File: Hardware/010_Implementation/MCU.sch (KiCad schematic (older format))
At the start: 21 parts, among them J1 2606-3356, J2 Conn_02x05_Odd_Even, SW1 SW_Push, U2 ESP32-DEVKITC-32D

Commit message: Board Version 5
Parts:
- C12, C13, C14, C15: footprint (none) -> Capacitor_SMD:C_0603_1608Metric_Pad1.08x0.95mm_HandSolder
- C8: footprint Capacitor_SMD:C_0603_1608Metric_Pad1.05x0.95mm_HandSolder -> Capacitor_SMD:C_0603_1608Metric_Pad1.08x0.95mm_HandSolder
- D2: Field4 2.65 mm -> (none)
- D3, D4, D5, SW1: Vorhanden (none) -> Yes
- J2: value Conn_02x05_Odd_Even -> JTAG Jumper Pins; Vorhanden (none) -> Yes
- R10, R11, R12, R13, R14, R15, R9: footprint Resistor_SMD:R_0805_2012Metric_Pad1.15x1.40mm_HandSolder -> Resistor_SMD:R_0603_1608Metric_Pad0.98x0.95mm_HandSolder
- R8: value 2.2k -> 1k; footprint Resistor_SMD:R_0805_2012Metric_Pad1.15x1.40mm_HandSolder -> Resistor_SMD:R_0603_1608Metric_Pad0.98x0.95mm_HandSolder
- U2: Field4 4 -> (none); Vorhanden (none) -> Yes
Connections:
- net OBD-CAN_Switch renamed ~OBD~\CAN
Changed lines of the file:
@@
 F 2 "Button_Switch_SMD:SW_Push_1P1T_NO_CK_KSC7xxJ" H 3525 6250 50  0001 C CNN
 F 3 "~" H 3525 6250 50  0001 C CNN
+F 4 "Yes" H 3525 6050 50  0001 C CNN "Vorhanden"
 	1    3525 6050
 	0    -1   -1   0
@@
 F 0 "C8" H 4265 6071 50  0000 L CNN
 F 1 "100n" H 4265 5980 50  0000 L CNN
-F 2 "Capacitor_SMD:C_0603_1608Metric_Pad1.05x0.95mm_HandSolder" H 4188 5875 50  0001 C CNN
+F 2 "Capacitor_SMD:C_0603_1608Metric_Pad1.08x0.95mm_HandSolder" H 4188 5875 50  0001 C CNN
 F 3 "~" H 4150 6025 50  0001 C CNN
 	1    4150 6025
@@
 P 9100 5025
 F 0 "J2" H 9150 4600 50  0000 C CNN
-F 1 "Conn_02x05_Odd_Even" H 9150 4691 50  0000 C CNN
+F 1 "JTAG Jumper Pins" H 9150 4691 50  0000 C CNN
 F 2 "Connector_PinHeader_1.00mm:PinHeader_2x05_P1.00mm_Vertical" H 9100 5025 50  0001 C CNN
 F 3 "~" H 9100 5025 50  0001 C CNN
+F 4 "Yes" H 9100 5025 50  0001 C CNN "Vorhanden"
 	1    9100 5025
 	-1   0    0    1
@@
 F 0 "R9" V 7468 4625 50  0000 C CNN
 F 1 "100" V 7559 4625 50  0000 C CNN
-F 2 "Resistor_SMD:R_0805_2012Metric_Pad1.15x1.40mm_HandSolder" V 7605 4625 50  0001 C CNN
+F 2 "Resistor_SMD:R_0603_1608Metric_Pad0.98x0.95mm_HandSolder" V 7605 4625 50  0001 C CNN
 F 3 "~" H 7675 4625 50  0001 C CNN
 	1    7675 4625
@@
 F 0 "R10" V 7468 4925 50  0000 C CNN
 F 1 "100" V 7559 4925 50  0000 C CNN
-F 2 "Resistor_SMD:R_0805_2012Metric_Pad1.15x1.40mm_HandSolder" V 7605 4925 50  0001 C CNN
+F 2 "Resistor_SMD:R_0603_1608Metric_Pad0.98x0.95mm_HandSolder" V 7605 4925 50  0001 C CNN
 F 3 "~" H 7675 4925 50  0001 C CNN
 	1    7675 4925
@@
 F 0 "R11" V 7882 5250 50  0000 C CNN
 F 1 "100" V 7791 5250 50  0000 C CNN
-F 2 "Resistor_SMD:R_0805_2012Metric_Pad1.15x1.40mm_HandSolder" V 7605 5250 50  0001 C CNN
+F 2 "Resistor_SMD:R_0603_1608Metric_Pad0.98x0.95mm_HandSolder" V 7605 5250 50  0001 C CNN
 F 3 "~" H 7675 5250 50  0001 C CNN
 	1    7675 5250
@@
 F 0 "R12" V 7882 5600 50  0000 C CNN
 F 1 "100" V 7791 5600 50  0000 C CNN
-F 2 "Resistor_SMD:R_0805_2012Metric_Pad1.15x1.40mm_HandSolder" V 7605 5600 50  0001 C CNN
+F 2 "Resistor_SMD:R_0603_1608Metric_Pad0.98x0.95mm_HandSolder" V 7605 5600 50  0001 C CNN
 F 3 "~" H 7675 5600 50  0001 C CNN
 	1    7675 5600
@@
 F 2 "LED_THT:LED_D3.0mm" H 7925 2325 50  0001 C CNN
 F 3 "~" H 7925 2325 50  0001 C CNN
+F 4 "Yes" H 7925 2325 50  0001 C CNN "Vorhanden"
 	1    7925 2325
 	0    -1   -1   0
@@
 F 2 "LED_THT:LED_D3.0mm" H 8350 2325 50  0001 C CNN
 F 3 "~" H 8350 2325 50  0001 C CNN
+F 4 "Yes" H 8350 2325 50  0001 C CNN "Vorhanden"
 	1    8350 2325
 	0    -1   -1   0
@@
 F 2 "LED_THT:LED_D3.0mm" H 8775 2325 50  0001 C CNN
 F 3 "~" H 8775 2325 50  0001 C CNN
+F 4 "Yes" H 8775 2325 50  0001 C CNN "Vorhanden"
 	1    8775 2325
 	0    -1   -1   0
@@
 F 0 "R13" H 7995 2846 50  0000 L CNN
 F 1 "500" H 7995 2755 50  0000 L CNN
-F 2 "Resistor_SMD:R_0805_2012Metric_Pad1.15x1.40mm_HandSolder" V 7855 2800 50  0001 C CNN
+F 2 "Resistor_SMD:R_0603_1608Metric_Pad0.98x0.95mm_HandSolder" V 7855 2800 50  0001 C CNN
 F 3 "~" H 7925 2800 50  0001 C CNN
 	1    7925 2800
@@
 F 0 "R14" H 8420 2846 50  0000 L CNN
 F 1 "500" H 8420 2755 50  0000 L CNN
-F 2 "Resistor_SMD:R_0805_2012Metric_Pad1.15x1.40mm_HandSolder" V 8280 2800 50  0001 C CNN
+F 2 "Resistor_SMD:R_0603_1608Metric_Pad0.98x0.95mm_HandSolder" V 8280 2800 50  0001 C CNN
 F 3 "~" H 8350 2800 50  0001 C CNN
 	1    8350 2800
@@
 F 0 "R15" H 8845 2846 50  0000 L CNN
 F 1 "500" H 8845 2755 50  0000 L CNN
-F 2 "Resistor_SMD:R_0805_2012Metric_Pad1.15x1.40mm_HandSolder" V 8705 2800 50  0001 C CNN
+F 2 "Resistor_SMD:R_0603_1608Metric_Pad0.98x0.95mm_HandSolder" V 8705 2800 50  0001 C CNN
 F 3 "~" H 8775 2800 50  0001 C CNN
 	1    8775 2800
@@
 F 1 "ESP32-DEVKITC-32D" H 3595 2085 50  0000 C CNN
 F 2 "Board:MODULE_ESP32-DEVKITC-32D" H 3600 3180 50  0001 L BNN
-F 3 "Espressif Systems" H 3600 3180 50  0001 L BNN
-F 4 "4" H 3600 3180 50  0001 L BNN "Field4"
+F 3 "https://www.espressif.com/sites/default/files/documentation/esp32_technical_reference_manual_en.pdf#603" H 3600 3180 50  0001 L BNN
+F 4 "" H 3600 3180 50  0001 L BNN "Field4"
+F 5 "Yes" H 3600 3180 50  0001 C CNN "Vorhanden"
 	1    3600 3180
 	1    0    0    1
@@
 OBD_Voltage_Check
 Text HLabel 1875 3180 0    50   Output ~ 0
-OBD-CAN_Switch
+~OBD~\CAN
 $Comp
 L Device:R R8
@@
 P 3525 5550
 F 0 "R8" H 3595 5596 50  0000 L CNN
-F 1 "2.2k" H 3595 5505 50  0000 L CNN
-F 2 "Resistor_SMD:R_0805_2012Metric_Pad1.15x1.40mm_HandSolder" V 3455 5550 50  0001 C CNN
+F 1 "1k" H 3595 5505 50  0000 L CNN
+F 2 "Resistor_SMD:R_0603_1608Metric_Pad0.98x0.95mm_HandSolder" V 3455 5550 50  0001 C CNN
 F 3 "~" H 3525 5550 50  0001 C CNN
 	1    3525 5550
@@
 F 1 "SS24" H 1665 1476 50  0000 C CNN
 F 2 "Board:DIOM5336X265N" H 1665 1350 50  0001 L BNN
-F 3 "IPC 7351B" H 1665 1350 50  0001 L BNN
-F 4 "2.65 mm" H 1665 1350 50  0001 L BNN "Field4"
+F 3 "https://www.onsemi.com/pub/Collateral/SS24-D.PDF" H 1665 1350 50  0001 L BNN
+F 4 "" H 1665 1350 50  0001 L BNN "Field4"
 F 5 "ON Semiconductor" H 1665 1350 50  0001 L BNN "Field5"
 F 6 "1.1.2" H 1665 1350 50  0001 L BNN "Field6"
@@
 F 1 "2606-3356" H 1567 4994 60  0000 C CNN
 F 2 "Board:2606-3356" H 1725 5415 60  0001 C CNN
-F 3 "" H 1325 6275 60  0000 C CNN
+F 3 "https://www.wago.com/global/pcb-terminal-blocks-and-pluggable-connectors/pcb-terminal-block/p/2606-3356" H 1325 6275 60  0001 C CNN
 	1    1325 6275
 	-1   0    0    1
@@
 F 0 "C14" H 4845 1601 50  0000 L CNN
 F 1 "100n" H 4845 1510 50  0000 L CNN
-F 2 "" H 4768 1405 50  0001 C CNN
+F 2 "Capacitor_SMD:C_0603_1608Metric_Pad1.08x0.95mm_HandSolder" H 4768 1405 50  0001 C CNN
 F 3 "~" H 4730 1555 50  0001 C CNN
 	1    4730 1555
@@
 F 0 "C15" H 5200 1601 50  0000 L CNN
 F 1 "1u" H 5200 1510 50  0000 L CNN
-F 2 "" H 5123 1405 50  0001 C CNN
+F 2 "Capacitor_SMD:C_0603_1608Metric_Pad1.08x0.95mm_HandSolder" H 5123 1405 50  0001 C CNN
 F 3 "~" H 5085 1555 50  0001 C CNN
 	1    5085 1555
@@
 F 0 "C13" H 2575 1741 50  0000 L CNN
 F 1 "100n" H 2575 1650 50  0000 L CNN
-F 2 "" H 2498 1545 50  0001 C CNN
+F 2 "Capacitor_SMD:C_0603_1608Metric_Pad1.08x0.95mm_HandSolder" H 2498 1545 50  0001 C CNN
 F 3 "~" H 2460 1695 50  0001 C CNN
 	1    2460 1695
@@
 F 0 "C12" H 1990 1741 50  0000 R CNN
 F 1 "1u" H 1990 1650 50  0000 R CNN
-F 2 "" H 2143 1545 50  0001 C CNN
+F 2 "Capacitor_SMD:C_0603_1608Metric_Pad1.08x0.95mm_HandSolder" H 2143 1545 50  0001 C CNN
 F 3 "~" H 2105 1695 50  0001 C CNN
 	1    2105 1695

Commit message: Board Version 7
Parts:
- removed J1: 2606-3356, Board:2606-3356, symbol Board-rescue:2606-3356-2020-11-09_14-09-29
- added J1: Conn_01x08_Female, Board:AST 045-08, symbol Connector:Conn_01x08_Female
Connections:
- net +3V3: now also J1.1 (Pin_1)
- net GND: now also J1.2 (Pin_2)
- net GPIO_1: now also J1.3 (Pin_3)
- net GPIO_2: now also J1.4 (Pin_4)
- net GPIO_3: now also J1.5 (Pin_5)
- net GPIO_4: now also J1.6 (Pin_6)
- no-connect marks 17 -> 13
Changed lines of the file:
@@
 GPIO_4
 Wire Wire Line
-	1325 5375 1925 5375
+	1325 5275 1925 5275
 Wire Wire Line
 	1325 5175 1925 5175
@@
 L power:GND #PWR012
 U 1 1 5F86CB8D
-P 1925 5375
-F 0 "#PWR012" H 1925 5125 50  0001 C CNN
-F 1 "GND" H 1930 5202 50  0000 C CNN
-F 2 "" H 1925 5375 50  0001 C CNN
-F 3 "" H 1925 5375 50  0001 C CNN
-	1    1925 5375
+P 1925 5275
+F 0 "#PWR012" H 1925 5025 50  0001 C CNN
+F 1 "GND" H 1930 5102 50  0000 C CNN
+F 2 "" H 1925 5275 50  0001 C CNN
+F 3 "" H 1925 5275 50  0001 C CNN
+	1    1925 5275
 	1    0    0    -1
 $EndComp
@@
 	775  4400 2125 4400
 Wire Wire Line
+	1325 5675 1675 5675
+Wire Wire Line
 	1325 5575 1675 5575
 Wire Wire Line
-	1325 5775 1675 5775
-Wire Wire Line
-	1325 5975 1675 5975
-Wire Wire Line
-	1325 6175 1675 6175
+	1325 5475 1675 5475
+Text Label 1675 5675 2    50   ~ 0
+GPIO_4
 Text Label 1675 5575 2    50   ~ 0
-GPIO_4
-Text Label 1675 5775 2    50   ~ 0
 GPIO_3
-Text Label 1675 5975 2    50   ~ 0
+Text Label 1675 5475 2    50   ~ 0
 GPIO_2
-Text Label 1675 6175 2    50   ~ 0
+Text Label 1680 5375 2    50   ~ 0
 GPIO_1
 Wire Wire Line
@@
 NoConn ~ 2800 3380
 $Comp
-L Board-rescue:2606-3356-2020-11-09_14-09-29 J1
-U 1 1 5FB5C146
-P 1325 6275
-AR Path="/5FB5C146" Ref="J1"  Part="1"
-AR Path="/5F52F099/5FB5C146" Ref="J1"  Part="1"
-F 0 "J1" H 1567 4888 60  0000 C CNN
-F 1 "2606-3356" H 1567 4994 60  0000 C CNN
-F 2 "Board:2606-3356" H 1725 5415 60  0001 C CNN
-F 3 "https://www.wago.com/global/pcb-terminal-blocks-and-pluggable-connectors/pcb-terminal-block/p/2606-3356" H 1325 6275 60  0001 C CNN
-	1    1325 6275
-	-1   0    0    1
-$EndComp
-NoConn ~ 1325 5275
-NoConn ~ 1325 5475
-NoConn ~ 1325 5675
-NoConn ~ 1325 5875
-NoConn ~ 1325 6075
-NoConn ~ 1325 6275
-$Comp
 L Device:C C14
 U 1 1 5FBFD557
@@
 Wire Wire Line
 	2460 1350 2800 1350
+Wire Wire Line
+	1680 5375 1325 5375
+$Comp
+L Connector:Conn_01x08_Female J1
+U 1 1 5FC7E1BA
+P 1125 5475
+F 0 "J1" H 1017 4850 50  0000 C CNN
+F 1 "Conn_01x08_Female" H 1017 4941 50  0000 C CNN
+F 2 "Board:AST 045-08" H 1125 5475 50  0001 C CNN
+F 3 "~" H 1125 5475 50  0001 C CNN
+	1    1125 5475
+	-1   0    0    -1
+$EndComp
+NoConn ~ 1325 5875
+NoConn ~ 1325 5775
 $EndSCHEMATC

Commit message: Board version 8 with gerber files
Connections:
- net Indicator_AP_Mode: now also U2.21 (IO19); no longer U2.22 (IO18)
- net Indicator_STA_Mode: now also U2.22 (IO18); no longer U2.21 (IO19)
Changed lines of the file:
@@
 Text Label 5125 3280 2    50   ~ 0
 WiFi_Mode
-Text Label 5125 3080 2    50   ~ 0
+Text Label 5125 3180 2    50   ~ 0
 Indicator_AP_Mode
-Text Label 5125 3180 2    50   ~ 0
-Indicator_STA_Mode
 Text Label 5125 2580 2    50   ~ 0
 Indicator_Error
@@
 	4400 2980 5125 2980
 Wire Wire Line
-	5125 3080 4400 3080
-Wire Wire Line
-	4400 3180 5125 3180
+	5125 3180 4400 3180
 Wire Wire Line
 	4400 3280 5125 3280
@@
 NoConn ~ 1325 5875
 NoConn ~ 1325 5775
+Wire Wire Line
+	4400 3080 5125 3080
+Text Label 5125 3080 2    50   ~ 0
+Indicator_STA_Mode
 $EndSCHEMATC

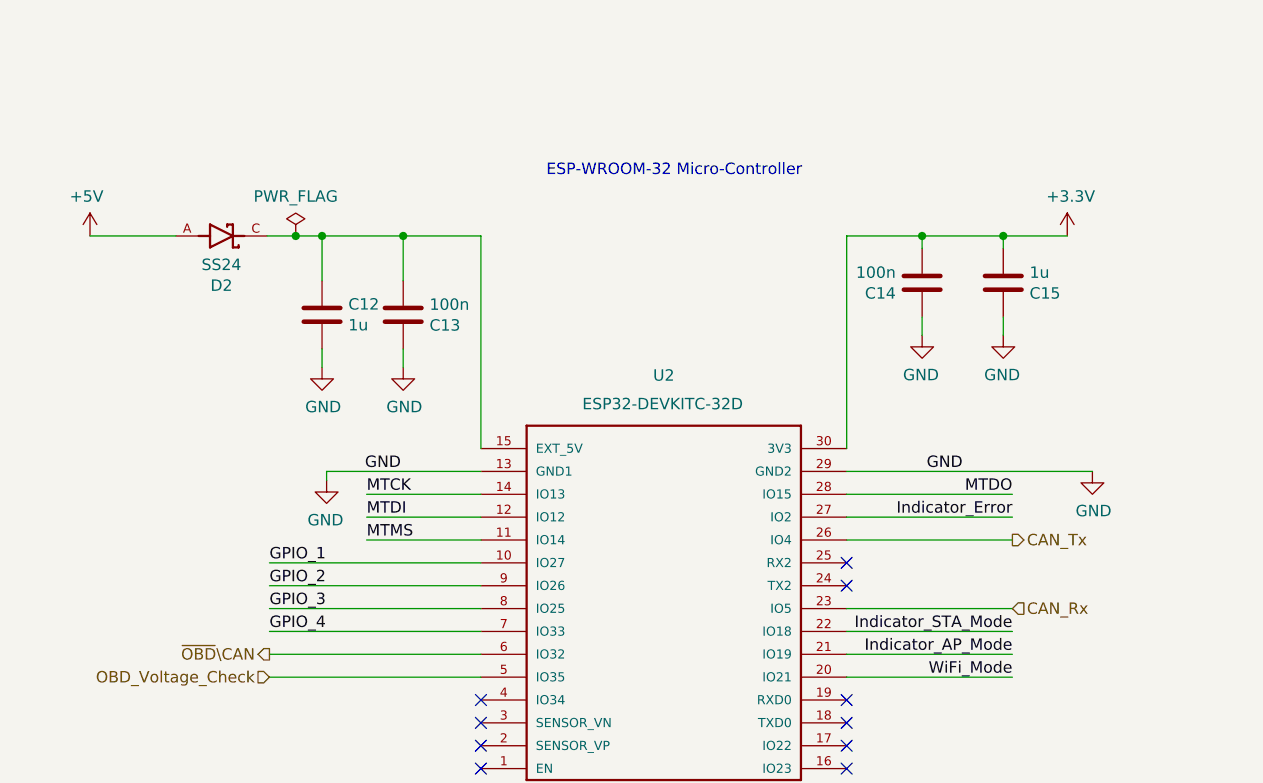
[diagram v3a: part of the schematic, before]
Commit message: Board Version 1.1 Fixed Relay Supply, standard Pins for CAN Transceiver and added CAN high and Low Labels
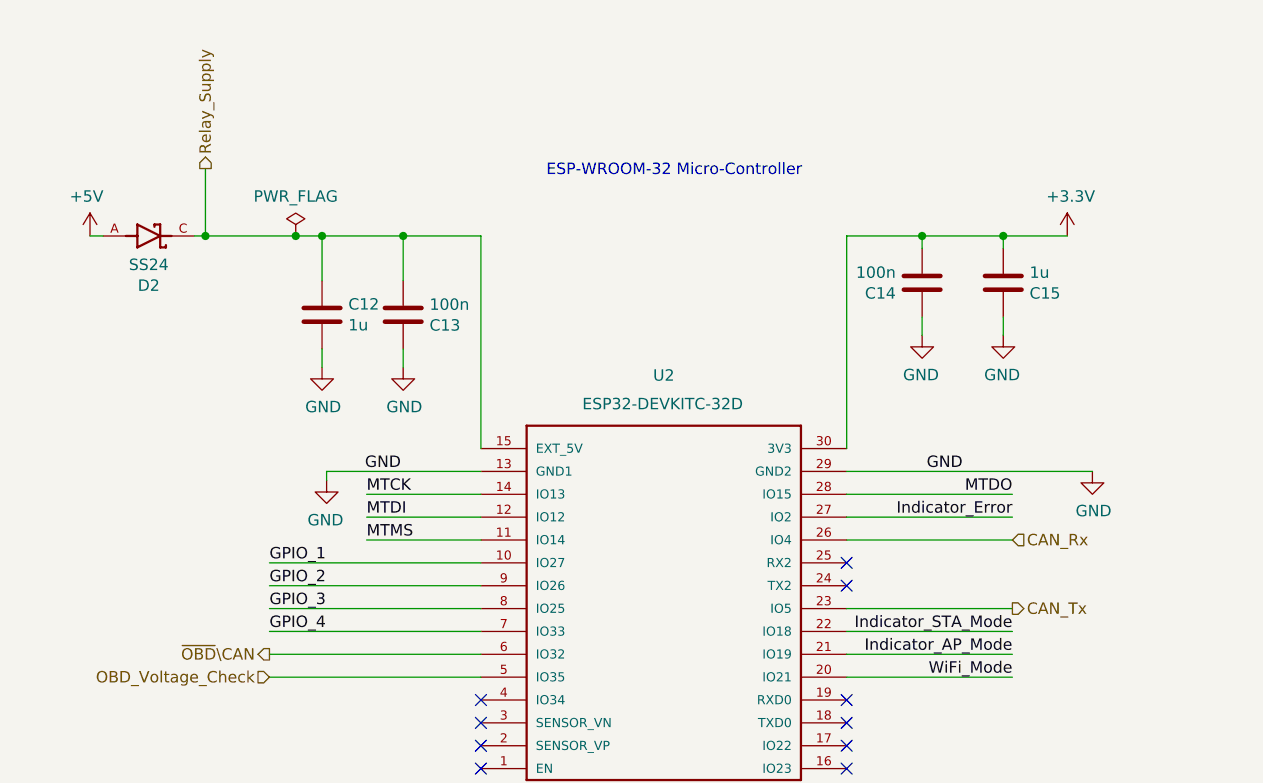
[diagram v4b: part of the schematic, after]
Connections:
- net CAN_Rx: now also U2.26 (IO4); no longer U2.23 (IO5)
- net CAN_Tx: now also U2.23 (IO5); no longer U2.26 (IO4)
- net Relay_Supply: now reaches C12.1, C13.2, D2.C, U2.15 (EXT_5V)
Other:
- moved on the sheet: D2
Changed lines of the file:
@@
 Text Notes 4050 4775 2    50   ~ 0
 WiFi-Mode Button
-Text HLabel 5125 2680 2    50   Output ~ 0
+Text HLabel 5125 2980 2    50   Output ~ 0
 CAN_Tx
-Text HLabel 5125 2980 2    50   Input ~ 0
+Text HLabel 5125 2680 2    50   Input ~ 0
 CAN_Rx
 Text Label 1875 2880 0    50   ~ 0
@@
 	4400 2580 5125 2580
 Wire Wire Line
-	5125 2680 4400 2680
-Wire Wire Line
-	4400 2980 5125 2980
+	5125 2980 4400 2980
+Wire Wire Line
+	4400 2680 5125 2680
 Wire Wire Line
 	5125 3180 4400 3180
@@
 L Board:SS24 D2
 U 1 1 5FB70E5B
-P 1665 1350
-F 0 "D2" H 1665 1567 50  0000 C CNN
-F 1 "SS24" H 1665 1476 50  0000 C CNN
-F 2 "Board:DIOM5336X265N" H 1665 1350 50  0001 L BNN
-F 3 "https://www.onsemi.com/pub/Collateral/SS24-D.PDF" H 1665 1350 50  0001 L BNN
-F 4 "" H 1665 1350 50  0001 L BNN "Field4"
-F 5 "ON Semiconductor" H 1665 1350 50  0001 L BNN "Field5"
-F 6 "1.1.2" H 1665 1350 50  0001 L BNN "Field6"
-	1    1665 1350
+P 1347 1350
+F 0 "D2" H 1347 1567 50  0000 C CNN
+F 1 "SS24" H 1347 1476 50  0000 C CNN
+F 2 "Board:DIOM5336X265N" H 1347 1350 50  0001 L BNN
+F 3 "https://www.onsemi.com/pub/Collateral/SS24-D.PDF" H 1347 1350 50  0001 L BNN
+F 4 "" H 1347 1350 50  0001 L BNN "Field4"
+F 5 "ON Semiconductor" H 1347 1350 50  0001 L BNN "Field5"
+F 6 "1.1.2" H 1347 1350 50  0001 L BNN "Field6"
+	1    1347 1350
 	1    0    0    1
 $EndComp
 Wire Wire Line
-	1865 1350 1990 1350
-Wire Wire Line
-	1465 1350 1090 1350
+	1547 1350 1595 1350
+Wire Wire Line
+	1147 1350 1090 1350
 $Comp
 L power:PWR_FLAG #FLG03
@@
 Text Label 5125 3080 2    50   ~ 0
 Indicator_STA_Mode
+Wire Wire Line
+	1595 1350 1595 1055
+Connection ~ 1595 1350
+Wire Wire Line
+	1595 1350 1990 1350
+Text HLabel 1595 1055 1    50   Output ~ 0
+Relay_Supply
 $EndSCHEMATC
